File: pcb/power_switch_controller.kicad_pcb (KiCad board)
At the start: 2 copper layers, 118.1 x 54.6 mm, 63 parts, among them P1 PWR_JACK_2.5x5.5, P2 HEADER_01X03, P3 BNC_DOUBLE_RA, P4 HEADER_02X08_SMD, P5 HEADER_02X08_SMD, P6 HEADER_02X08_SMD, P7 HEADER_02X08_SMD, SW1 DPST_SERIES_M, SW2 KT_SWITCH, U1 MAX6817, U2 MAX6817, U3 TLE723X, U4 TLE723X, U5 TLE723X, U6 TLE723X

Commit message: Progress towards pcb v1.4.
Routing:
- net GND: track 449.0 -> 0.00 mm, vias 3 -> 0
- net VAA: track 270.6 -> 0.00 mm, vias 4 -> 0
- net +5V: track 254.0 -> 0.00 mm, vias 4 -> 0
- net /SCK: track 203.9 -> 0.00 mm, vias 1 -> 0
- net /LED_PWR: track 151.6 -> 0.00 mm, vias 1 -> 0
- net /RST: track 151.1 -> 0.00 mm, vias 6 -> 0
- net /CS: track 137.5 -> 0.00 mm, vias 5 -> 0
- net /IN: track 131.6 -> 0.00 mm, vias 3 -> 0
- net /ENC_B: track 101.7 -> 0.00 mm, vias 1 -> 0
- net /MOSI: track 101.7 -> 0.00 mm, vias 1 -> 0
- net /TX3: track 98.5 -> 0.00 mm
- net /MISO: track 91.2 -> 0.00 mm
- net /V_IN: track 69.5 -> 0.00 mm
- net /BNC_B: track 63.0 -> 0.00 mm
- net /BNC_A: track 56.3 -> 0.00 mm, vias 1 -> 0
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- removed copper zone on B.Cu, net GND
- removed copper zone on F.Cu, net VAA

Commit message: Updated bom.
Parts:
- removed C8, C9: 0.1uF, power_switch_controller:SM1210
- removed E1: ENCODER_C14, power_switch_controller:Micro-MaTch_6_SMD
- removed R1, R2: 5.11k, power_switch_controller:SM1210
- removed S1: HEADER_01X02_SHR, power_switch_controller:Header_Shrouded_2_Pin
- removed SW2: KT_SWITCH, power_switch_controller:KT_SWITCH
- removed U5, U6: TLE723X, power_switch_controller:TLE723X
- added P10: HEADER_02X08_SMD, power_switch_controller:HEADER_02x08_SMD, F.Cu at (160.0, 111.8)
- added P11: HEADER_02X08_SMD, power_switch_controller:HEADER_02x08_SMD, F.Cu at (129.5, 111.8)
- added P8: HEADER_02X08_SMD, power_switch_controller:HEADER_02x08_SMD, F.Cu at (160.0, 88.9)
- added P9: HEADER_02X08_SMD, power_switch_controller:HEADER_02x08_SMD, F.Cu at (129.5, 88.9)
- P2: value HEADER_01X03 -> HEADER_01X03_SMD_RA; footprint footprints:Header_3_Pin -> power_switch_controller:Header_3_Pin_SMD_RA
- P3: value BNC_DOUBLE_RA -> HEADER_01X03_SMD_RA; footprint power_switch_controller:BNC_DOUBLE -> power_switch_controller:Header_3_Pin_SMD_RA; moved to B.Cu
- P4: value HEADER_02X08_SMD -> HEADER_01X03_SMD_RA; footprint power_switch_controller:HEADER_02x08_SMD -> power_switch_controller:Header_3_Pin_SMD_RA
- P5: value HEADER_02X08_SMD -> HEADER_01X03_SMD_RA; footprint power_switch_controller:HEADER_02x08_SMD -> power_switch_controller:Header_3_Pin_SMD_RA; moved to B.Cu
- P6: value HEADER_02X08_SMD -> HEADER_01X02_SMD_RA; footprint power_switch_controller:HEADER_02x08_SMD -> power_switch_controller:Header_2_Pin_SMD_RA
- P7: value HEADER_02X08_SMD -> BNC_DOUBLE_RA; footprint power_switch_controller:HEADER_02x08_SMD -> power_switch_controller:BNC_DOUBLE
- SW1: value DPST_SERIES_M -> SPST_SLIDE_AS; footprint power_switch_controller:DPST_SERIES_M -> power_switch_controller:SPST_SLIDE_AS
- U1, U2: value MAX6817 -> TLE723X; footprint power_switch_controller:MAX6817 -> power_switch_controller:TLE723X
- moved P3 107.4 mm to (203.8, 79.4), turned to 180 degrees
- moved C2 100.7 mm to (104.8, 108.6), turned to 180 degrees
- moved REG1 96.6 mm to (103.5, 113.0), turned to 180 degrees
- moved P5 83.2 mm to (203.8, 126.4)
- moved C5 58.2 mm to (142.2, 87.0), turned to 270 degrees
- moved U2 53.5 mm to (129.5, 87.0), turned to 180 degrees
- moved P4 49.0 mm to (208.9, 85.1), turned to 270 degrees
- moved P6 46.6 mm to (203.8, 127.6), turned to 180 degrees
- moved P2 37.6 mm to (96.1, 85.2), turned to 90 degrees
- moved P7 31.7 mm to (99.1, 102.9), turned to 90 degrees
- moved D1 26.1 mm to (201.9, 94.0)
- moved SW1 23.0 mm to (203.2, 112.4), turned to 90 degrees
- moved C7 22.9 mm to (142.2, 109.9)
- moved U3 22.9 mm to (160.0, 109.9)
- moved U4 22.9 mm to (129.5, 109.9)
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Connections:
- ARDUINO1 pad 0: Net-(ARDUINO1-Pad0) -> /RX0
- ARDUINO1 pad 1: Net-(ARDUINO1-Pad1) -> /TX0
- ARDUINO1 pad 10: Net-(ARDUINO1-Pad10) -> (no net)
- ARDUINO1 pad 11: Net-(ARDUINO1-Pad11) -> (no net)
- ARDUINO1 pad 12: Net-(ARDUINO1-Pad12) -> (no net)
- ARDUINO1 pad 13: Net-(ARDUINO1-Pad13) -> (no net)
- ARDUINO1 pad 15: Net-(ARDUINO1-Pad15) -> /RX3
- ARDUINO1 pad 16: Net-(ARDUINO1-Pad16) -> /TX2
- ARDUINO1 pad 17: /D_LIGHTS -> /RX2
- ARDUINO1 pad 18: /ENC_A -> /TX1
- ARDUINO1 pad 19: /D_ENC_BTN -> /RX1
- ARDUINO1 pad 2: /ENC_B -> (no net)
- ARDUINO1 pad 20: /D_SWITCH -> (no net)
- ARDUINO1 pad 20B: Net-(ARDUINO1-Pad20B) -> (no net)
- ARDUINO1 pad 21: /D_BTN -> (no net)
- ARDUINO1 pad 21B: Net-(ARDUINO1-Pad21B) -> (no net)
- ARDUINO1 pad 22: Net-(ARDUINO1-Pad22) -> (no net)
- ARDUINO1 pad 23: Net-(ARDUINO1-Pad23) -> (no net)
- ARDUINO1 pad 24: Net-(ARDUINO1-Pad24) -> (no net)
- ARDUINO1 pad 25: Net-(ARDUINO1-Pad25) -> (no net)
- ARDUINO1 pad 26: Net-(ARDUINO1-Pad26) -> (no net)
- ARDUINO1 pad 27: Net-(ARDUINO1-Pad27) -> (no net)
- ARDUINO1 pad 28: Net-(ARDUINO1-Pad28) -> (no net)
- ARDUINO1 pad 29: Net-(ARDUINO1-Pad29) -> (no net)
- ARDUINO1 pad 30: Net-(ARDUINO1-Pad30) -> (no net)
- ARDUINO1 pad 31: Net-(ARDUINO1-Pad31) -> (no net)
- ARDUINO1 pad 32: Net-(ARDUINO1-Pad32) -> (no net)
- ARDUINO1 pad 33: Net-(ARDUINO1-Pad33) -> (no net)
- ARDUINO1 pad 34: Net-(ARDUINO1-Pad34) -> (no net)
- ARDUINO1 pad 35: Net-(ARDUINO1-Pad35) -> (no net)
- ARDUINO1 pad 36: Net-(ARDUINO1-Pad36) -> (no net)
- ARDUINO1 pad 37: Net-(ARDUINO1-Pad37) -> (no net)
- ARDUINO1 pad 38: Net-(ARDUINO1-Pad38) -> (no net)
- ARDUINO1 pad 39: Net-(ARDUINO1-Pad39) -> (no net)
- ARDUINO1 pad 3V3: Net-(ARDUINO1-Pad3V3) -> (no net)
- ARDUINO1 pad 4: Net-(ARDUINO1-Pad4) -> (no net)
- ARDUINO1 pad 40: Net-(ARDUINO1-Pad40) -> (no net)
- ARDUINO1 pad 41: Net-(ARDUINO1-Pad41) -> (no net)
- ARDUINO1 pad 42: Net-(ARDUINO1-Pad42) -> (no net)
- ARDUINO1 pad 43: Net-(ARDUINO1-Pad43) -> (no net)
- ARDUINO1 pad 44: Net-(ARDUINO1-Pad44) -> (no net)
- ARDUINO1 pad 45: Net-(ARDUINO1-Pad45) -> (no net)
- ARDUINO1 pad 46: Net-(ARDUINO1-Pad46) -> /CS
- ARDUINO1 pad 47: Net-(ARDUINO1-Pad47) -> (no net)
- ARDUINO1 pad 48: /IN -> /BNC_A
- ARDUINO1 pad 49: /CS -> (no net)
- ARDUINO1 pad 5: Net-(ARDUINO1-Pad5) -> (no net)
- ARDUINO1 pad 53: Net-(ARDUINO1-Pad53) -> (no net)
- ARDUINO1 pad 5V_5: Net-(ARDUINO1-Pad5V_5) -> (no net)
- ARDUINO1 pad 6: Net-(ARDUINO1-Pad6) -> (no net)
- ARDUINO1 pad 7: Net-(ARDUINO1-Pad7) -> (no net)
- ARDUINO1 pad 8: Net-(ARDUINO1-Pad8) -> (no net)
- ARDUINO1 pad 9: Net-(ARDUINO1-Pad9) -> (no net)
- ARDUINO1 pad A0: /BNC_A -> (no net)
- ARDUINO1 pad A1: Net-(ARDUINO1-PadA1) -> (no net)
- ARDUINO1 pad A10: Net-(ARDUINO1-PadA10) -> (no net)
- ARDUINO1 pad A11: Net-(ARDUINO1-PadA11) -> (no net)
- ARDUINO1 pad A12: Net-(ARDUINO1-PadA12) -> (no net)
- ARDUINO1 pad A13: Net-(ARDUINO1-PadA13) -> (no net)
- ARDUINO1 pad A14: Net-(ARDUINO1-PadA14) -> (no net)
- ARDUINO1 pad A15: Net-(ARDUINO1-PadA15) -> (no net)
- ARDUINO1 pad A2: Net-(ARDUINO1-PadA2) -> (no net)
- ARDUINO1 pad A3: Net-(ARDUINO1-PadA3) -> (no net)
- ARDUINO1 pad A4: Net-(ARDUINO1-PadA4) -> (no net)
- ARDUINO1 pad A5: Net-(ARDUINO1-PadA5) -> (no net)
- ARDUINO1 pad A6: Net-(ARDUINO1-PadA6) -> (no net)
- ARDUINO1 pad A7: Net-(ARDUINO1-PadA7) -> (no net)
- ARDUINO1 pad A8: Net-(ARDUINO1-PadA8) -> (no net)
- ARDUINO1 pad A9: Net-(ARDUINO1-PadA9) -> (no net)
- ARDUINO1 pad AREF: Net-(ARDUINO1-PadAREF) -> (no net)
- ARDUINO1 pad GND3: Net-(ARDUINO1-PadGND3) -> (no net)
- ARDUINO1 pad GND4: Net-(ARDUINO1-PadGND4) -> (no net)
- ARDUINO1 pad GND5: Net-(ARDUINO1-PadGND5) -> (no net)
- ARDUINO1 pad IREF: Net-(ARDUINO1-PadIREF) -> (no net)
- ARDUINO1 pad NC: Net-(ARDUINO1-PadNC) -> (no net)
- C2 pad 1: /V_IN -> VAA
- C3 pad 1: +5V -> /V_IN
- C4 pad 1: +5VD -> +5V
- C5 pad 1: +5VD -> +5V
- P2 pad 1: /TX3 -> /RX0
- P2 pad 3: +5V -> /TX0
- P3 pad 1: /BNC_A -> /RX1
- P3 pad 3: /BNC_B -> /TX1
- P4 pad 1: VAA -> /RX2
- P4 pad 2: /OUT0 -> GND
- P4 pad 3: VAA -> /TX2
- P5 pad 1: VAA -> /RX3
- P5 pad 2: /OUT8 -> GND
- P5 pad 3: VAA -> /TX3
- P6 pad 1: VAA -> GND
- P6 pad 2: /OUT16 -> +5VD
- P7 pad 1: VAA -> /BNC_A
- P7 pad 2: /OUT24 -> GND
- P7 pad 3: VAA -> /BNC_B
- P7 pad 4: /OUT25 -> GND
- U1 pad 1: /ENC_BTN -> /CS
- U1 pad 3: /LIGHTS -> /OUT2
- U1 pad 4: /D_LIGHTS -> /OUT3
- U1 pad 5: +5VD -> GND
- U1 pad 6: /D_ENC_BTN -> GND
- U2 pad 1: /BTN -> /CS
- U2 pad 3: /SWITCH -> /OUT10
- U2 pad 4: /D_SWITCH -> /OUT11
- U2 pad 5: +5VD -> GND
- U2 pad 6: /D_BTN -> GND
- U3 pad 10: /OUT5 -> /OUT21
- U3 pad 12: /SI1 -> /SI3
- U3 pad 14: /MOSI -> /SI2
- U3 pad 15: /OUT6 -> /OUT22
- U3 pad 16: /OUT7 -> /OUT23
- U3 pad 2: /IN -> GND
- U3 pad 21: /OUT0 -> /OUT16
- U3 pad 22: /OUT1 -> /OUT17
- U3 pad 3: /OUT2 -> /OUT18
- U3 pad 4: /OUT3 -> /OUT19
- U3 pad 9: /OUT4 -> /OUT20
- U4 pad 10: /OUT13 -> /OUT29
- U4 pad 12: /SI2 -> /MISO
- U4 pad 14: /SI1 -> /SI3
- U4 pad 15: /OUT14 -> /OUT30
- U4 pad 16: /OUT15 -> /OUT31
- U4 pad 2: /IN -> GND
- U4 pad 21: /OUT8 -> /OUT24
- U4 pad 22: /OUT9 -> /OUT25
- U4 pad 3: /OUT10 -> /OUT26
- U4 pad 4: /OUT11 -> /OUT27
- U4 pad 9: /OUT12 -> /OUT28
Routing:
- net GND: track 0.00 -> 472.6 mm, vias 0 -> 3
- net VAA: track 0.00 -> 246.7 mm, vias 0 -> 3
- net /RST: track 0.00 -> 212.6 mm, vias 0 -> 3
- net +5V: track 0.00 -> 202.4 mm, vias 0 -> 3
- net /LED_PWR: track 0.00 -> 189.4 mm
- net /CS: track 0.00 -> 132.3 mm, vias 0 -> 2
- net /SCK: track 0.00 -> 128.0 mm, vias 0 -> 4
- net /BNC_A: track 0.00 -> 107.0 mm
- net /MISO: track 0.00 -> 75.2 mm, vias 0 -> 1
- net /RX0: track 0.00 -> 68.4 mm
- net /MOSI: track 0.00 -> 65.0 mm, vias 0 -> 1
- net +5VD: track 0.00 -> 64.2 mm
- net /V_IN: track 0.00 -> 62.9 mm
- net /BNC_B: track 0.00 -> 61.9 mm
- net /TX3: track 0.00 -> 61.6 mm, vias 0 -> 1
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- added copper zone on B.Cu, net GND
- added copper zone on F.Cu, net VAA
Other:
- board size 118.1 x 54.6 mm -> 118.1 x 55.1 mm
- board text added: "12V"
- board text added: "Janelia Modular Device power_switch_controller model_number: 1110 02/2016 ver 1.4"
- board text added: "Lights"
- board text added: "Serial0"
- board text added: "Serial1"
- board text added: "Serial2"
- board text added: "Serial3"
- board text removed: "12V_DC_DC"
- board text removed: "DISPLAY"
- board text removed: "Janelia Modular Device power_switch_controller model_number: 1110 08/2015 version 1.3"
- board text removed: "SWITCH"

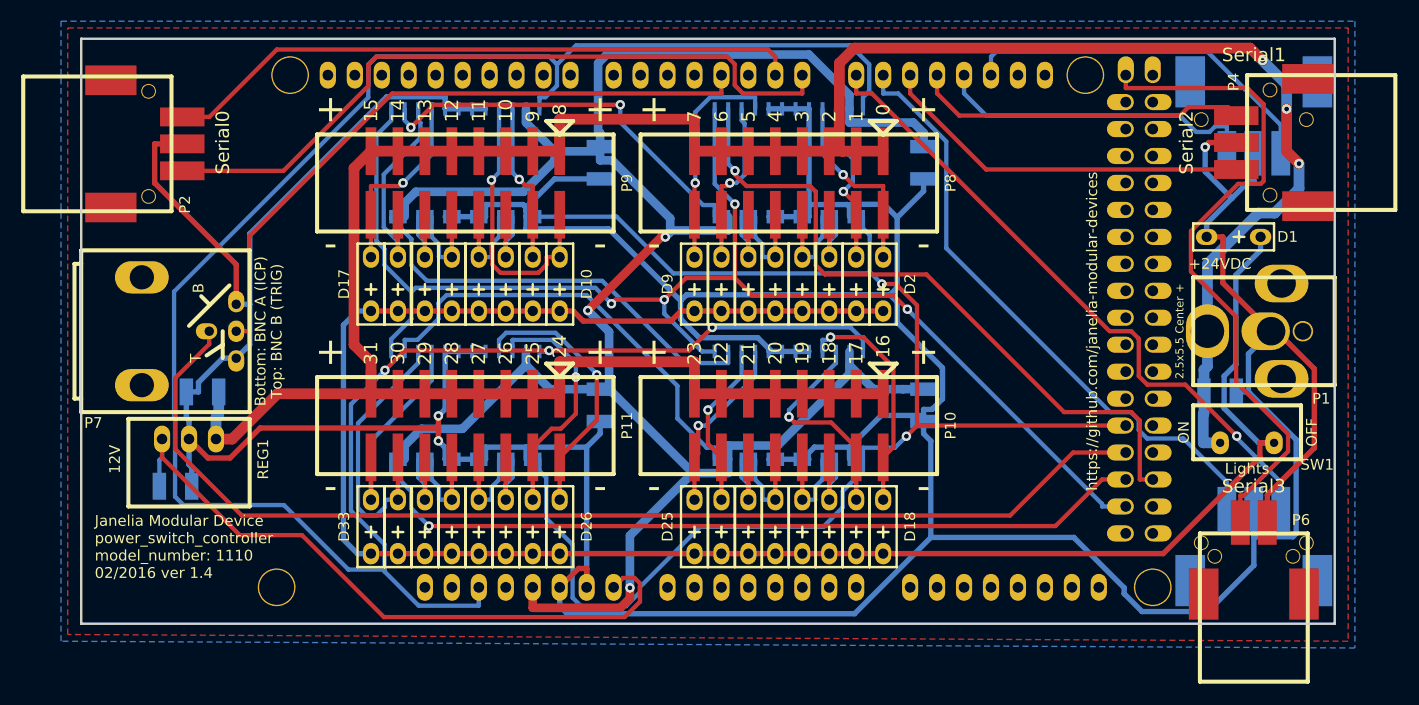
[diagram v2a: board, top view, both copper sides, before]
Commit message: Added TLE5X.
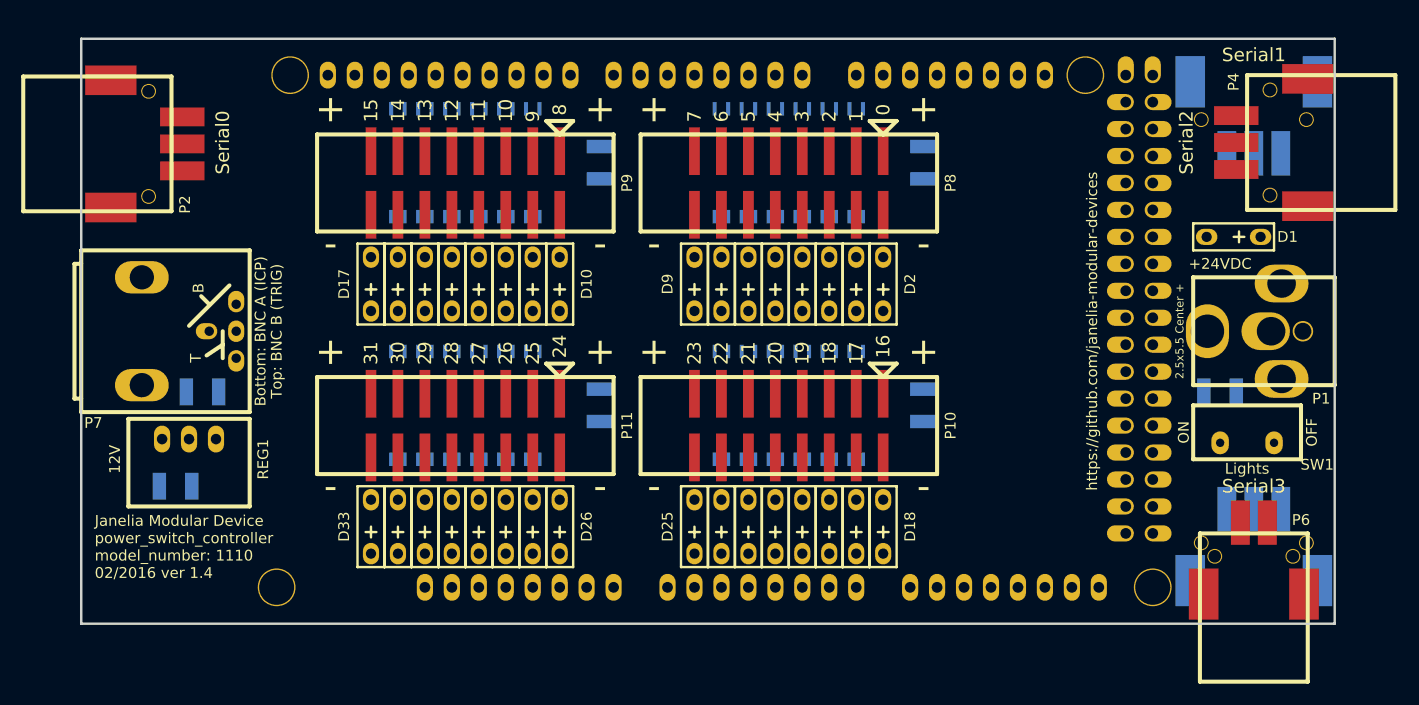
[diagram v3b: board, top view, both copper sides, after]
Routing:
- net GND: track 472.6 -> 0.00 mm, vias 3 -> 0
- net VAA: track 246.7 -> 0.00 mm, vias 3 -> 0
- net /RST: track 212.6 -> 0.00 mm, vias 3 -> 0
- net +5V: track 202.4 -> 0.00 mm, vias 3 -> 0
- net /LED_PWR: track 189.4 -> 0.00 mm
- net /CS: track 132.3 -> 0.00 mm, vias 2 -> 0
- net /SCK: track 128.0 -> 0.00 mm, vias 4 -> 0
- net /BNC_A: track 107.0 -> 0.00 mm
- net /MISO: track 75.2 -> 0.00 mm, vias 1 -> 0
- net /RX0: track 68.4 -> 0.00 mm
- net /MOSI: track 65.0 -> 0.00 mm, vias 1 -> 0
- net +5VD: track 64.2 -> 0.00 mm
- net /V_IN: track 62.9 -> 0.00 mm
- net /BNC_B: track 61.9 -> 0.00 mm
- net /TX3: track 61.6 -> 0.00 mm, vias 1 -> 0
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- removed copper zone on B.Cu, net GND
- removed copper zone on F.Cu, net VAA

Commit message: Finished pcb v1.5.
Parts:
- U1, U2, U3, U4: value TLE723X -> TLE7230R; footprint power_switch_controller:TLE723X -> power_switch_controller:PG-DSO-36
- moved U1 20.4 mm to (180.3, 88.9), turned to 270 degrees
- moved U3 20.4 mm to (180.3, 111.8), turned to 270 degrees
- moved U2 15.4 mm to (144.8, 88.9), turned to 270 degrees
- moved U4 15.4 mm to (144.8, 111.8), turned to 270 degrees
- moved C4 15.4 mm to (180.3, 100.3), turned to 0 degrees
- moved C6 15.4 mm to (180.3, 123.2), turned to 0 degrees
- moved C5 13.6 mm to (144.8, 100.3), turned to 0 degrees
- moved C7 13.6 mm to (144.8, 123.2), turned to 0 degrees
- moved D10 2.54 mm to (135.9, 98.4)
- moved D21 2.54 mm to (163.8, 121.3)
- moved D24 2.54 mm to (156.2, 121.3)
- moved D26 2.54 mm to (135.9, 121.3)
- moved D5 2.54 mm to (163.8, 98.4)
- moved D8 2.54 mm to (156.2, 98.4)
- moved D14 2.54 mm to (125.7, 98.4)
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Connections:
- ARDUINO1 pad 44: (no net) -> /RESET
- ARDUINO1 pad 5V_4: +5VD -> (no net)
- ARDUINO1 pad RST: /RST -> (no net)
- P6 pad 2: +5VD -> VAA
- U1 pad 1: /CS -> GND
- U1 pad 10: /OUT5 -> /CS
- U1 pad 11: +5V -> (no net)
- U1 pad 12: /SI1 -> GND
- U1 pad 13: /SCK -> GND
- U1 pad 14: /MOSI -> /OUT2
- U1 pad 15: /OUT6 -> /OUT3
- U1 pad 16: /OUT7 -> (no net)
- U1 pad 17: GND -> (no net)
- U1 pad 2: GND -> (no net)
- U1 pad 20: GND -> (no net)
- U1 pad 21: /OUT0 -> (no net)
- U1 pad 22: /OUT1 -> /OUT4
- U1 pad 23: +5V -> /OUT5
- U1 pad 24: /RST -> (no net)
- U1 pad 3: /OUT2 -> (no net)
- U1 pad 4: /OUT3 -> /OUT0
- U1 pad 5: GND -> /OUT1
- U1 pad 8: GND -> +5V
- U1 pad 9: /OUT4 -> /RESET
- U2 pad 1: /CS -> GND
- U2 pad 10: /OUT13 -> /CS
- U2 pad 11: +5V -> (no net)
- U2 pad 12: /SI2 -> GND
- U2 pad 13: /SCK -> GND
- U2 pad 14: /SI1 -> /OUT10
- U2 pad 15: /OUT14 -> /OUT11
- U2 pad 16: /OUT15 -> (no net)
- U2 pad 17: GND -> (no net)
- U2 pad 2: GND -> (no net)
- U2 pad 20: GND -> (no net)
- U2 pad 21: /OUT8 -> (no net)
- U2 pad 22: /OUT9 -> /OUT12
- U2 pad 23: +5V -> /OUT13
- U2 pad 24: /RST -> (no net)
- U2 pad 3: /OUT10 -> (no net)
- U2 pad 4: /OUT11 -> /OUT8
- U2 pad 5: GND -> /OUT9
- U2 pad 8: GND -> +5V
- U2 pad 9: /OUT12 -> /RESET
- U3 pad 1: /CS -> GND
- U3 pad 10: /OUT21 -> /CS
- U3 pad 11: +5V -> (no net)
- U3 pad 12: /SI3 -> GND
- U3 pad 13: /SCK -> GND
- U3 pad 14: /SI2 -> /OUT18
- U3 pad 15: /OUT22 -> /OUT19
- U3 pad 16: /OUT23 -> (no net)
- U3 pad 17: GND -> (no net)
- U3 pad 2: GND -> (no net)
- U3 pad 20: GND -> (no net)
- U3 pad 21: /OUT16 -> (no net)
- U3 pad 22: /OUT17 -> /OUT20
- U3 pad 23: +5V -> /OUT21
- U3 pad 24: /RST -> (no net)
- U3 pad 3: /OUT18 -> (no net)
- U3 pad 4: /OUT19 -> /OUT16
- U3 pad 5: GND -> /OUT17
- U3 pad 8: GND -> +5V
- U3 pad 9: /OUT20 -> /RESET
- U4 pad 1: /CS -> GND
- U4 pad 10: /OUT29 -> /CS
- U4 pad 11: +5V -> (no net)
- U4 pad 12: /MISO -> GND
- U4 pad 13: /SCK -> GND
- U4 pad 14: /SI3 -> /OUT26
- U4 pad 15: /OUT30 -> /OUT27
- U4 pad 16: /OUT31 -> (no net)
- U4 pad 17: GND -> (no net)
- U4 pad 2: GND -> (no net)
- U4 pad 20: GND -> (no net)
- U4 pad 21: /OUT24 -> (no net)
- U4 pad 22: /OUT25 -> /OUT28
- U4 pad 23: +5V -> /OUT29
- U4 pad 24: /RST -> (no net)
- U4 pad 3: /OUT26 -> (no net)
- U4 pad 4: /OUT27 -> /OUT24
- U4 pad 5: GND -> /OUT25
- U4 pad 8: GND -> +5V
- U4 pad 9: /OUT28 -> /RESET
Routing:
- net GND: track 0.00 -> 558.3 mm, vias 0 -> 1
- net VAA: track 0.00 -> 217.8 mm, vias 0 -> 1
- net +5V: track 0.00 -> 216.2 mm, vias 0 -> 4
- net /LED_PWR: track 0.00 -> 207.8 mm, vias 0 -> 1
- net /SCK: track 0.00 -> 112.7 mm, vias 0 -> 5
- net /RESET: track 0.00 -> 97.9 mm, vias 0 -> 1
- net /CS: track 0.00 -> 96.8 mm, vias 0 -> 2
- net /BNC_A: track 0.00 -> 91.3 mm
- net /TX3: track 0.00 -> 85.3 mm
- net /RX0: track 0.00 -> 70.0 mm
- net /RX3: track 0.00 -> 65.1 mm, vias 0 -> 1
- net /MISO: track 0.00 -> 62.2 mm, vias 0 -> 1
- net /SO2: track 0.00 -> 61.2 mm
- net /TX0: track 0.00 -> 58.4 mm
- net /BNC_B: track 0.00 -> 56.7 mm
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- added copper zone on B.Cu, net GND
- added copper zone on F.Cu, net VAA
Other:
- net class Default: clearance 0.254 -> 0.0254
- net class GND: clearance 0.254 -> 0.1016; trace_width 0.508 -> 0.4064
- net class SIGNAL: clearance 0.254 -> 0.1016
- rule trace_clearance: 0.254 -> 0.0254
- board text added: "Janelia Modular Device power_switch_controller model_number: 1110 03/2016 ver 1.5"
- board text removed: "Janelia Modular Device power_switch_controller model_number: 1110 02/2016 ver 1.4"
